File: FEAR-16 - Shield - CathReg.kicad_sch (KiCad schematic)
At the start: 7 parts, among them J101 Supply, J102 Signals, J103 Channel-In

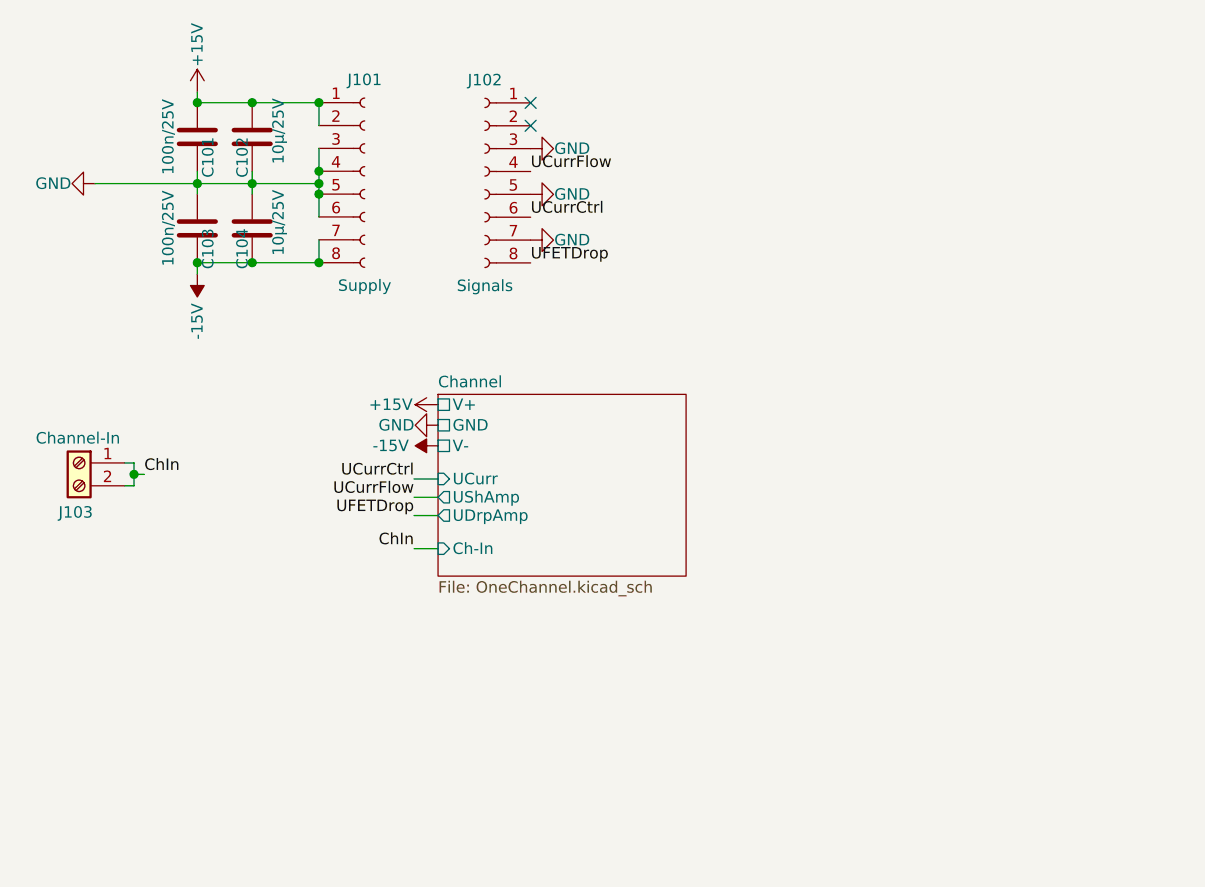
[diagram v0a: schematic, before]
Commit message: V1.3 (improved fine-tuning of CF- and UD-Amps)
PCB Changes:
 - Amplification Poti (1Meg) changed to Offset-Resistor (100k) + Poti (50k) to achieve 20x finer tuning of the amplification

Misc.:
 - Fixed .gitignore to ignore the prl files
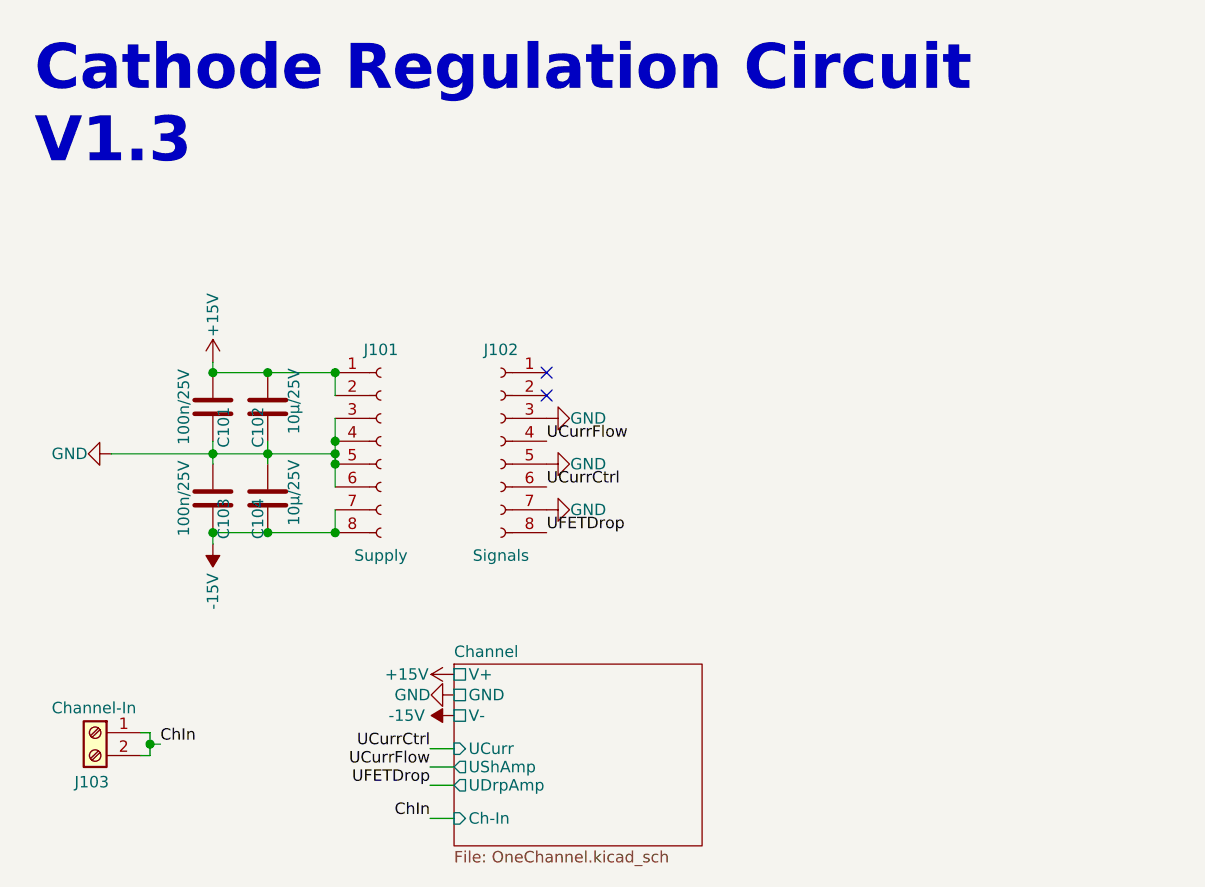
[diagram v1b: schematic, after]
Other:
- note added: "Cathode Regulation Circuit V1.3"
- moved on the sheet: C101, C102, C103, C104, J101, J102, J103
